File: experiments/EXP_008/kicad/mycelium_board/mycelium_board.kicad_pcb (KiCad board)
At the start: 2 copper layers, 56 parts, among them U1 ?, U10 ?, U11 ?, U12 ?, U13 ?, U14 ?, U15 ?, U16 ?, U17 ?, U18 ?, U19 ?, U2 ?, U20 ?, U21 ?, U22 ?, U23 ?, U24 ?, U25 ?, U26 ?, U27 ?, U28 ?, U29 ?, U3 ?, U30 ?, U31 ?, U32 ?, U33 ?, U34 ?, U35 ?, U36 ?, U37 ?, U38 ?, U39 ?, U4 ?, U40 ?, U41 ?, U42 ?, U43 ?, U44 ?, U45 ?, U46 ?, U47 ?, U48 ?, U49 ?, U5 ?, U50 ?, U51 ?, U52 ?, U53 ?, U54 ?, U55 ?, U56 ?, U6 ?, U7 ?, U8 ?, U9 ?

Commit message: chore: update fab-planner submodule, deploy workflow, and accumulated changes
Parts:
- moved U41 55.3 mm to (80.0, 114.0), turned to 180 degrees
- moved U11 15.8 mm to (75.5, 64.0), turned to 90 degrees

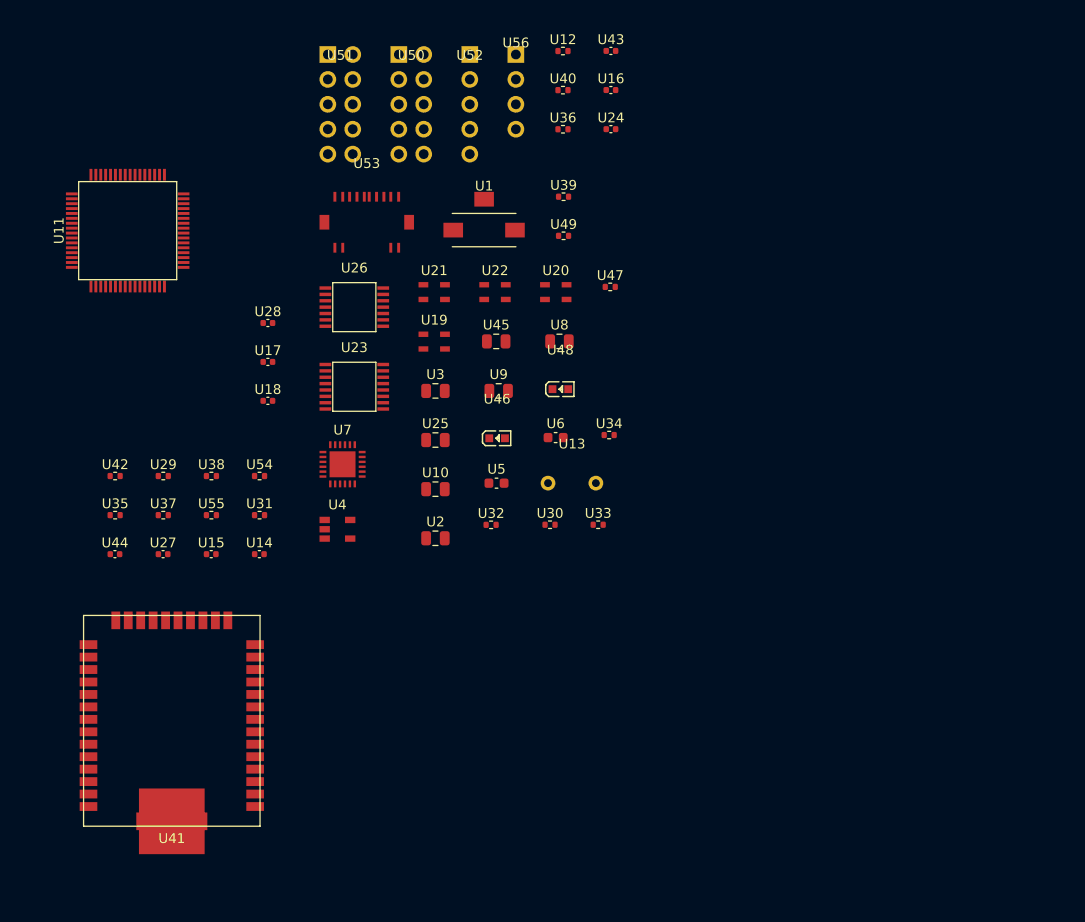
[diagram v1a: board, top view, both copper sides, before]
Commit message: feat: surface LattePanda dashboard URL in knowledge base Quick Access tables
- Added Quick Access section to structure.md with machine controller URL first
- Added Quick Access section to summary.md for project overview
- Updated software.md last updated date
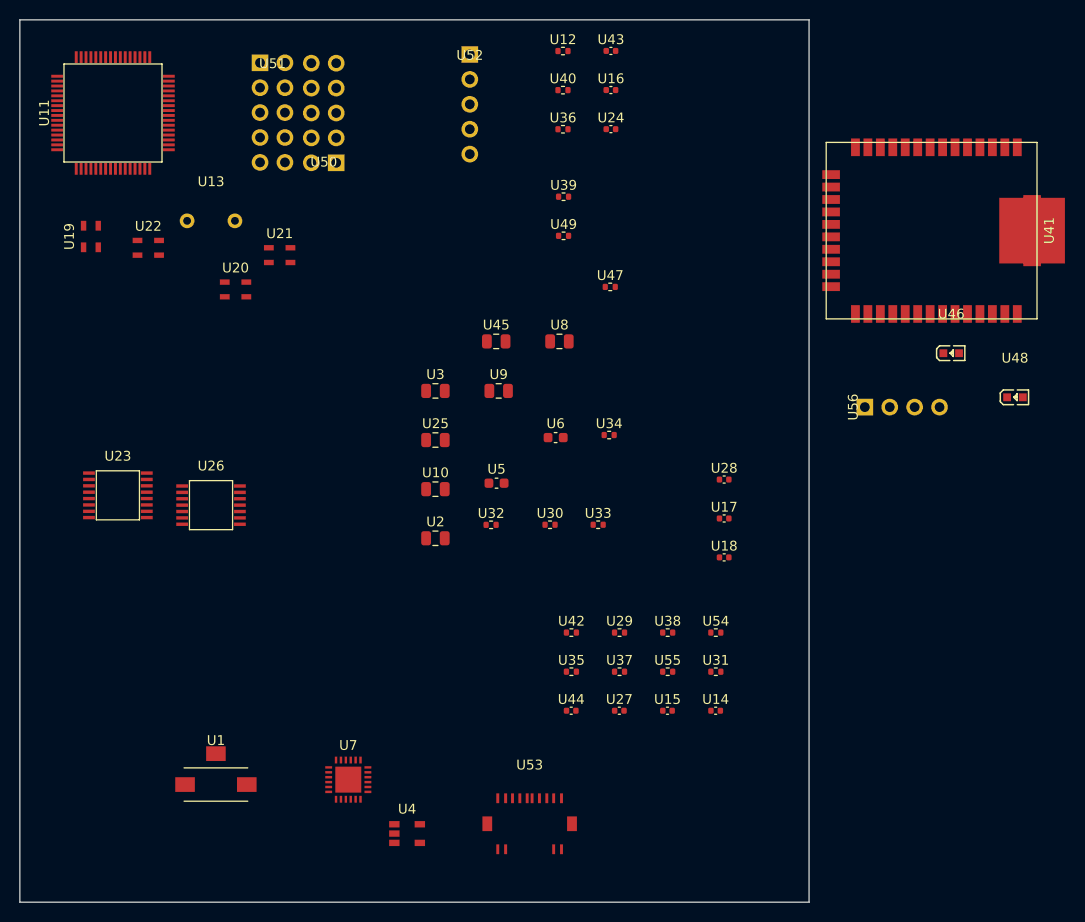
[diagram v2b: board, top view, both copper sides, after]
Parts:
- moved U41 92.2 mm to (157.5, 64.0), turned to -90 degrees
- moved U53 63.6 mm to (116.5, 124.5)
- moved U1 62.8 mm to (84.5, 120.5)
- moved U56 50.9 mm to (154.5, 82.0), turned to 90 degrees
- moved U15 49.2 mm to (130.6, 113.0)
- moved U17 49.2 mm to (136.3, 93.4)
- moved U18 49.2 mm to (136.3, 97.3)
- moved U27 49.2 mm to (125.7, 113.0)
- moved U28 49.2 mm to (136.3, 89.4)
- moved U29 49.2 mm to (125.7, 105.0)
- moved U31 49.2 mm to (135.5, 109.0)
- moved U35 49.2 mm to (120.8, 109.0)
- moved U37 49.2 mm to (125.7, 109.0)
- moved U38 49.2 mm to (130.6, 105.0)
- moved U42 49.2 mm to (120.8, 105.0)
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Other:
- board outline added: 80.5 x 90 mm
- copper layers 2 -> 4
